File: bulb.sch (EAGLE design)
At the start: 9 parts, among them U1 RFD22102, U2 IC REG LDO 3.3V

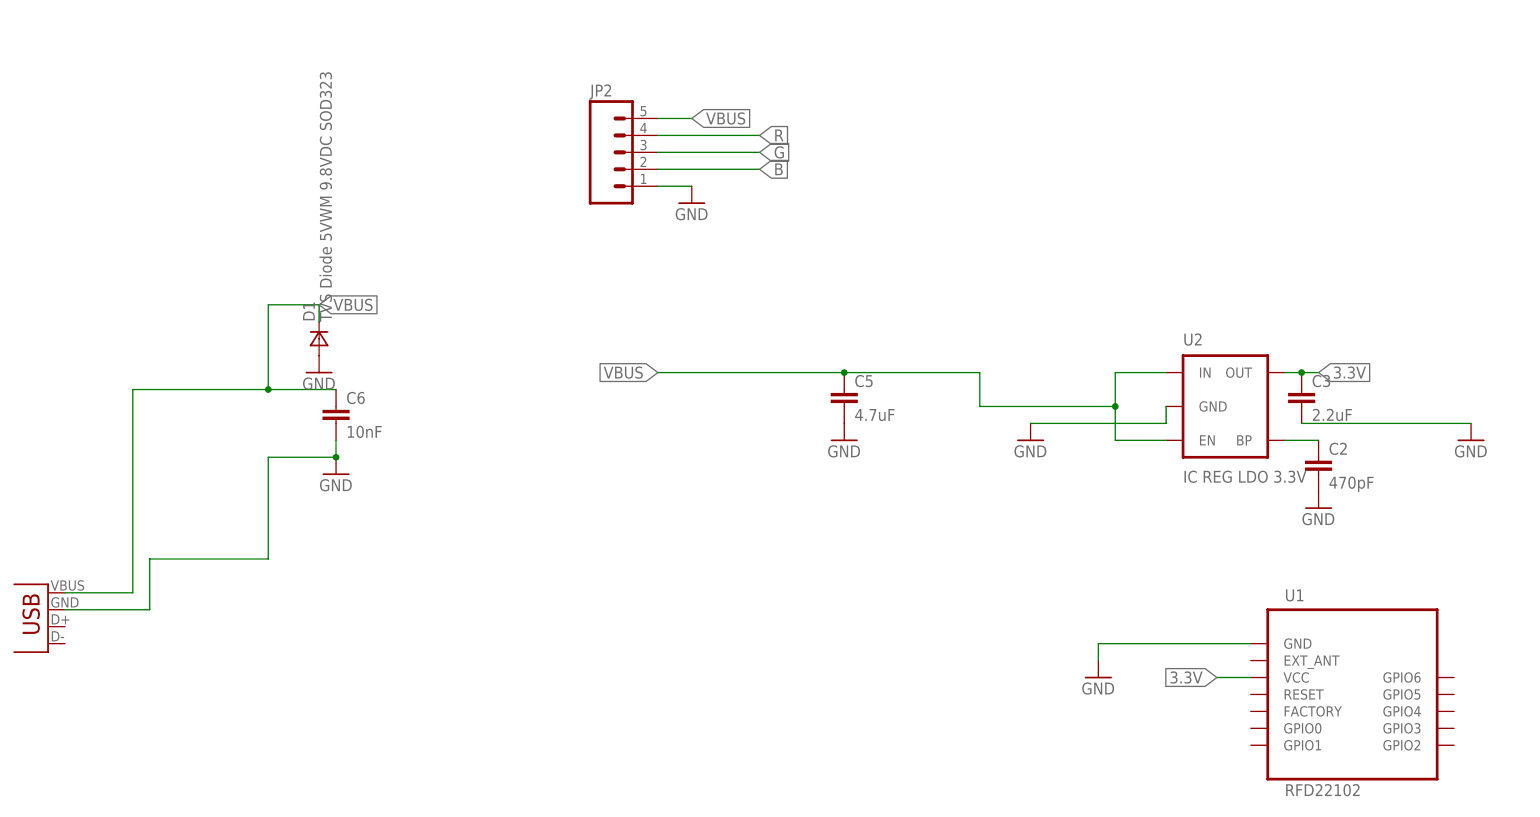
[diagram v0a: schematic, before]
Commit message: circle pcb, and updated usb pcb
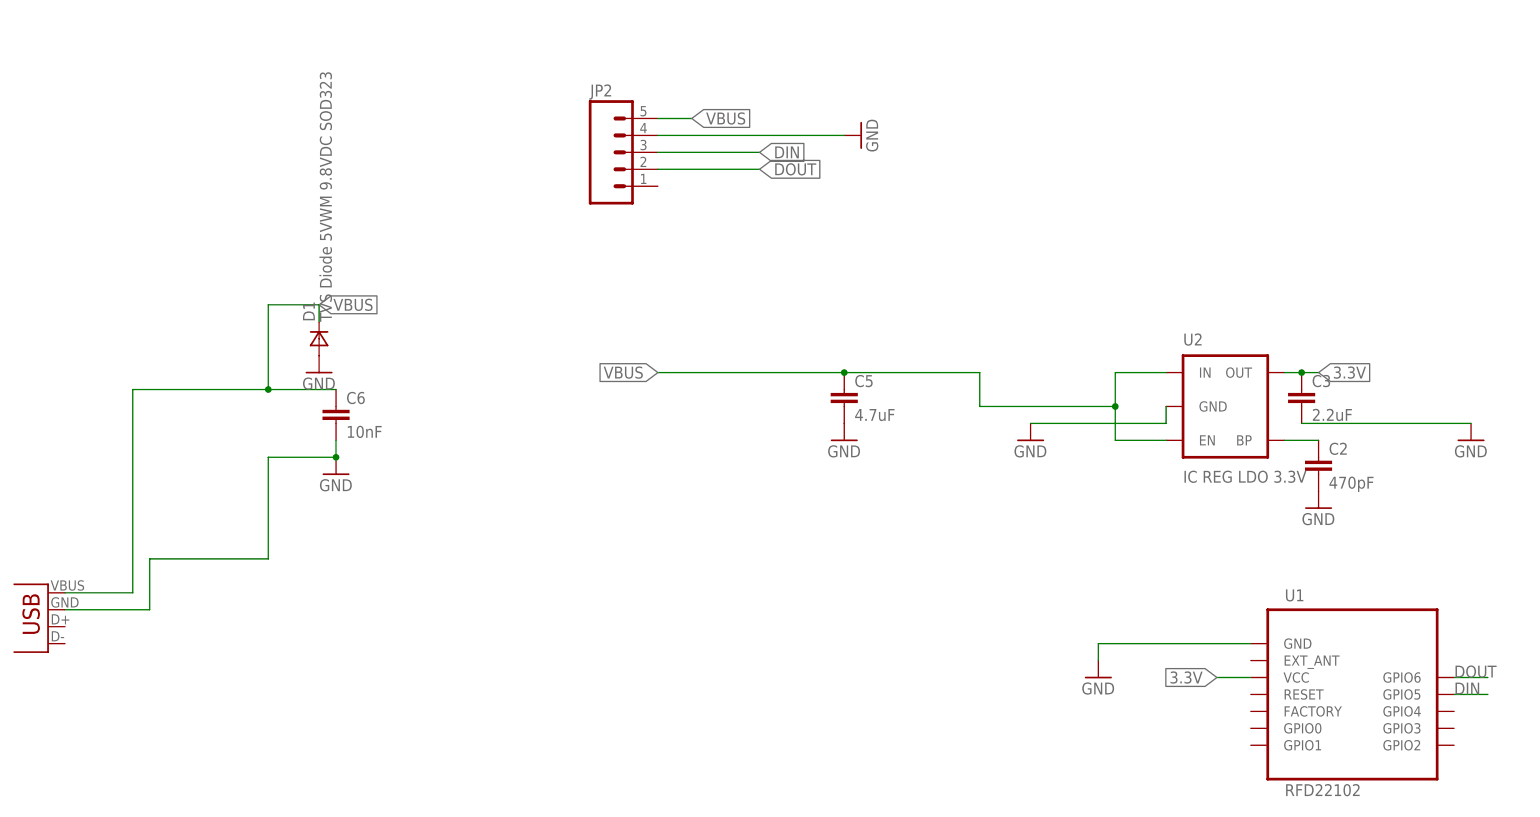
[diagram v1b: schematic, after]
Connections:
- removed net B: JP2.2
- removed net G: JP2.3
- removed net R: JP2.4
- new net DIN: JP2.3, U1.GPIO5
- new net DOUT: JP2.2, U1.GPIO6
- net GND: now also JP2.4; no longer JP2.1
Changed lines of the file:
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@@
 <part name="JP1" library="SparkFun-Connectors" deviceset="USB" device="-A-H"/>
 <part name="JP2" library="SparkFun-Connectors" deviceset="M05" device="PTH"/>
-<part name="CPY1" library="supply1" deviceset="GND" device=""/>
 <part name="U1" library="RF_Digital_RFD22102_Eagle_Schematic_PCB_Library" deviceset="RFD22102" device=""/>
 <part name="GND1" library="supply1" deviceset="GND" device=""/>
+<part name="CPY1" library="supply1" deviceset="GND" device=""/>
 </parts>
 <sheets>
@@
 <instance part="JP1" gate="G$1" x="35.56" y="86.36" rot="R180"/>
 <instance part="JP2" gate="G$1" x="119.38" y="152.4"/>
-<instance part="CPY1" gate="1" x="132.08" y="144.78"/>
 <instance part="U1" gate="G$1" x="231.14" y="71.12"/>
 <instance part="GND1" gate="1" x="193.04" y="73.66"/>
+<instance part="CPY1" gate="1" x="157.48" y="154.94" rot="R90"/>
 </instances>
 <busses>
@@
 </segment>
 <segment>
-<pinref part="JP2" gate="G$1" pin="1"/>
-<wire x1="127" y1="147.32" x2="132.08" y2="147.32" width="0.1524" layer="91"/>
-<pinref part="CPY1" gate="1" pin="GND"/>
-</segment>
-<segment>
 <pinref part="U1" gate="G$1" pin="GND"/>
 <wire x1="215.9" y1="78.74" x2="193.04" y2="78.74" width="0.1524" layer="91"/>
 <pinref part="GND1" gate="1" pin="GND"/>
 <wire x1="193.04" y1="78.74" x2="193.04" y2="76.2" width="0.1524" layer="91"/>
+</segment>
+<segment>
+<pinref part="JP2" gate="G$1" pin="4"/>
+<wire x1="127" y1="154.94" x2="154.94" y2="154.94" width="0.1524" layer="91"/>
+<pinref part="CPY1" gate="1" pin="GND"/>
 </segment>
 </net>
@@
 </segment>
 </net>
-<net name="R" class="0">
+<net name="DIN" class="0">
 <segment>
-<pinref part="JP2" gate="G$1" pin="4"/>
-<label x="142.24" y="154.94" size="1.778" layer="95" xref="yes"/>
-<wire x1="127" y1="154.94" x2="142.24" y2="154.94" width="0.1524" layer="91"/>
+<pinref part="U1" gate="G$1" pin="GPIO5"/>
+<wire x1="246.38" y1="71.12" x2="251.46" y2="71.12" width="0.1524" layer="91"/>
+<label x="246.38" y="71.12" size="1.778" layer="95"/>
 </segment>
-</net>
-<net name="G" class="0">
 <segment>
 <pinref part="JP2" gate="G$1" pin="3"/>
@@
 </segment>
 </net>
-<net name="B" class="0">
+<net name="DOUT" class="0">
+<segment>
+<pinref part="U1" gate="G$1" pin="GPIO6"/>
+<wire x1="246.38" y1="73.66" x2="251.46" y2="73.66" width="0.1524" layer="91"/>
+<label x="246.38" y="73.66" size="1.778" layer="95"/>
+</segment>
 <segment>
 <pinref part="JP2" gate="G$1" pin="2"/>

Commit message: updated pcbs
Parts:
- added R1: 470, resistor:R-US_R0603
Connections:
- removed net DIN: JP2.3, U1.GPIO5
- new net DIN-H: JP2.3, R1.1
- new net DIN-RF: R1.2, U1.GPIO5
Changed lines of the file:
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@@
 <part name="GND1" library="supply1" deviceset="GND" device=""/>
 <part name="CPY1" library="supply1" deviceset="GND" device=""/>
+<part name="R1" library="resistor" deviceset="R-US_" device="R0603" value="470"/>
 </parts>
 <sheets>
@@
 <instance part="GND1" gate="1" x="193.04" y="73.66"/>
 <instance part="CPY1" gate="1" x="157.48" y="154.94" rot="R90"/>
+<instance part="R1" gate="G$1" x="193.04" y="152.4"/>
 </instances>
 <busses>
@@
 </segment>
 </net>
-<net name="DIN" class="0">
-<segment>
-<pinref part="U1" gate="G$1" pin="GPIO5"/>
-<wire x1="246.38" y1="71.12" x2="251.46" y2="71.12" width="0.1524" layer="91"/>
-<label x="246.38" y="71.12" size="1.778" layer="95"/>
-</segment>
-<segment>
-<pinref part="JP2" gate="G$1" pin="3"/>
-<label x="142.24" y="152.4" size="1.778" layer="95" xref="yes"/>
-<wire x1="127" y1="152.4" x2="142.24" y2="152.4" width="0.1524" layer="91"/>
-</segment>
-</net>
 <net name="DOUT" class="0">
 <segment>
@@
 </segment>
 </net>
+<net name="DIN-H" class="0">
+<segment>
+<pinref part="R1" gate="G$1" pin="1"/>
+<wire x1="187.96" y1="152.4" x2="182.88" y2="152.4" width="0.1524" layer="91"/>
+<label x="182.88" y="152.4" size="1.778" layer="95"/>
+</segment>
+<segment>
+<pinref part="JP2" gate="G$1" pin="3"/>
+<wire x1="127" y1="152.4" x2="142.24" y2="152.4" width="0.1524" layer="91"/>
+<label x="142.24" y="152.4" size="1.778" layer="95"/>
+</segment>
+</net>
+<net name="DIN-RF" class="0">
+<segment>
+<pinref part="R1" gate="G$1" pin="2"/>
+<wire x1="198.12" y1="152.4" x2="203.2" y2="152.4" width="0.1524" layer="91"/>
+<label x="200.66" y="152.4" size="1.778" layer="95"/>
+</segment>
+<segment>
+<pinref part="U1" gate="G$1" pin="GPIO5"/>
+<wire x1="246.38" y1="71.12" x2="251.46" y2="71.12" width="0.1524" layer="91"/>
+<label x="246.38" y="71.12" size="1.778" layer="95"/>
+</segment>
+</net>
